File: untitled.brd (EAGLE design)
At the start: 54 x 54 mm, 26 parts, among them IC1 SN65220DBV, J3 CORTEX_DEBUG_PTH, J4 2X6 FEMALE, J6 USB-MICROB, U1 ATSAMD21G-M, U2 MIC5501-3.0YM5-TR, Y1 32.768kHz

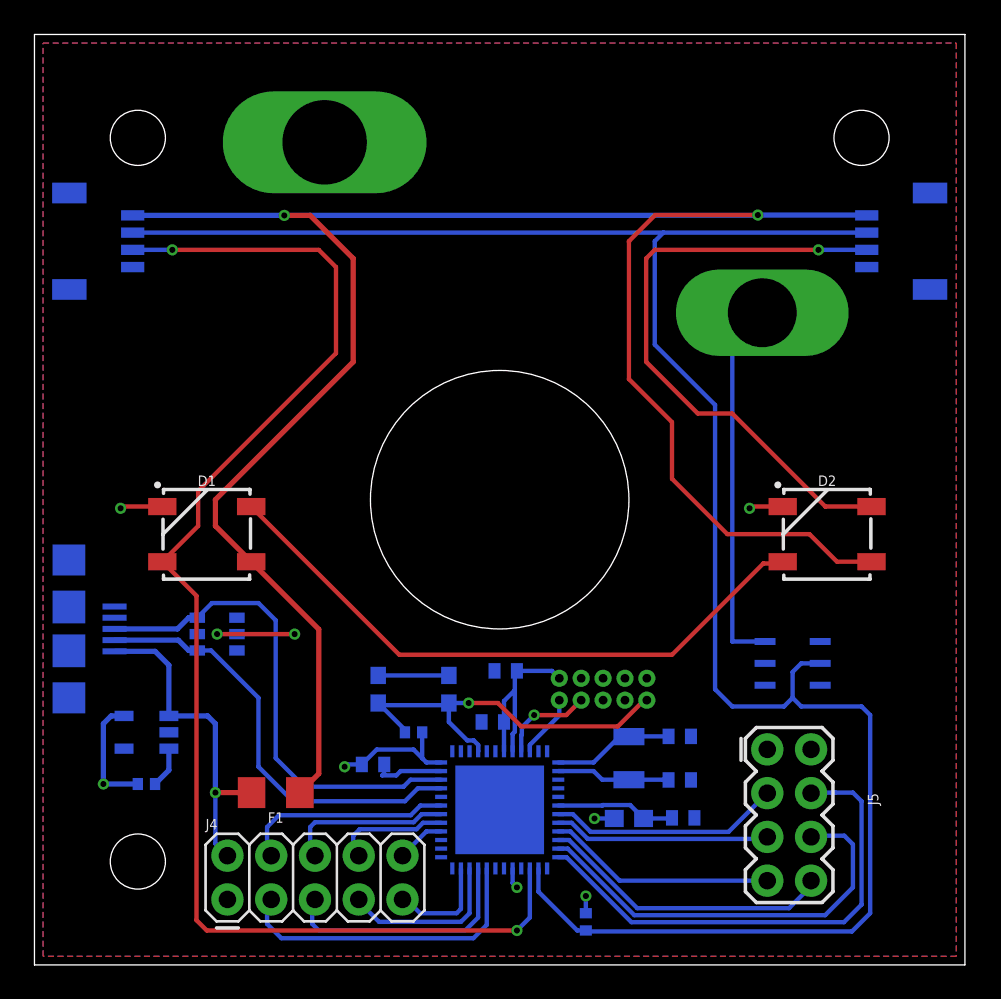
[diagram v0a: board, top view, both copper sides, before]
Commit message: corrected button orientation
placed novelkey on the correct side. reduced gpio by 2 pins to allow for tolerances. added mounting hole. updated routing.
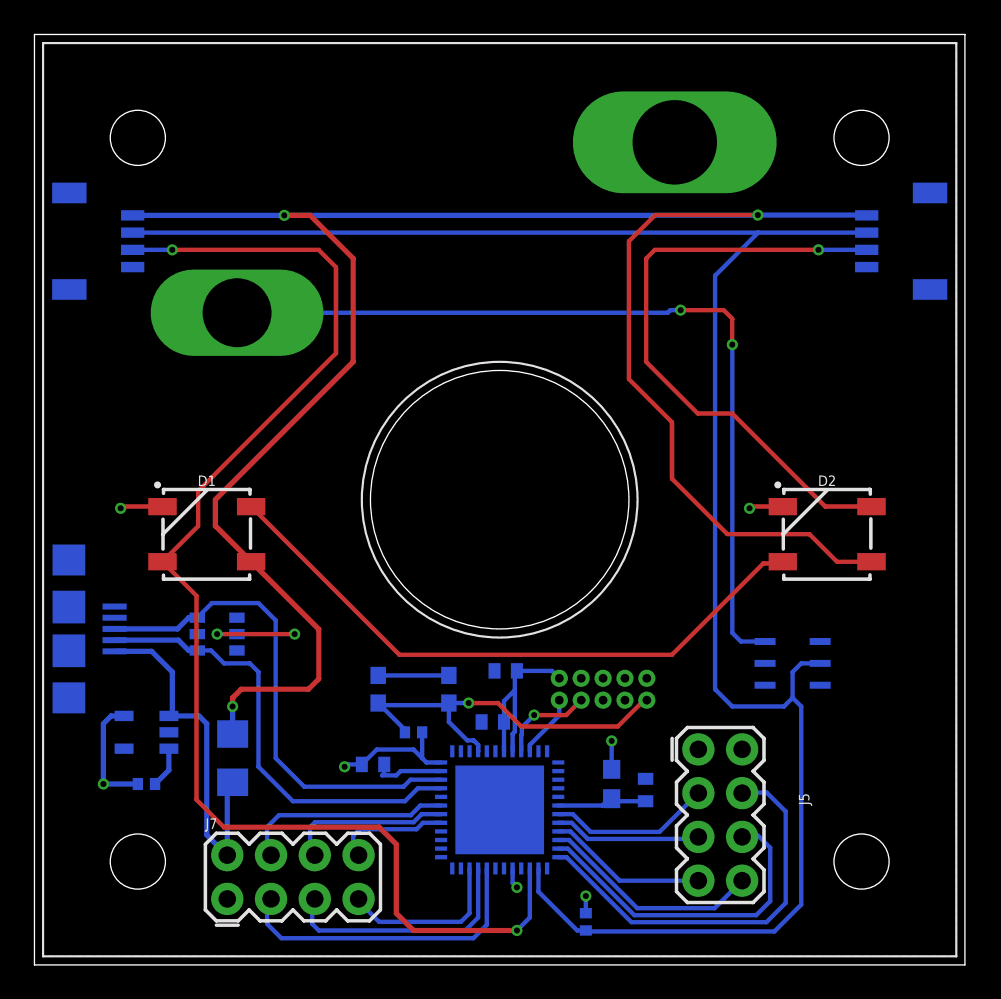
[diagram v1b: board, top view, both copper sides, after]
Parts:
- removed C4, C5: 12.5pf, resistor:C0402
- removed J4: 2X6 FEMALE, SparkFun-Connectors:2X5
- removed Y1: 32.768kHz, SparkFun-Clocks-custom:CRYSTAL-SMD-3.2X1.5MM
- added J7: (no value), SparkFun-Connectors:2X4
- moved J5 4.00 mm to (39.8, 8.70)
- moved F1 3.20 mm to (11.5, 12.0), flipped to the bottom, turned to 270 degrees
- moved C3 2.72 mm to (35.5, 10.2), turned to 90 degrees
- moved FB1 2.24 mm to (33.5, 10.5), turned to 270 degrees
- flipped U$1 to the top
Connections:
- removed net N$5: C4.1, U1.1, Y1.P$2
- removed net N$6: C5.1, U1.2, Y1.P$1
- removed net PA14: J4.9, U1.23
- removed net PA19: J4.10, U1.28
- net GND: now also J7.1; no longer C4.2, C5.2, J4.1
- net PA12: now also J7.5; no longer J4.5
- net PA13: now also J7.7; no longer J4.7
- net PA20: now also J7.8; no longer J4.8
- net PA21: now also J7.6; no longer J4.6
- net PA22: now also J7.4; no longer J4.4
- net PB11: now also J7.3; no longer J4.3
- net VBUS: now also J7.2; no longer J4.2
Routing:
- net N$10: track 21.7 -> 49.3 mm, vias 0 -> 2
- net 1W: track 117.6 -> 109.0 mm
- net N$5: track 7.03 -> 0.00 mm
- net N$6: track 6.61 -> 0.00 mm
- net PA14: track 6.17 -> 0.00 mm
- net PA06: track 24.5 -> 19.3 mm
- net PA07: track 28.7 -> 23.5 mm
- net PA05: track 17.2 -> 13.0 mm
- net PA09: track 12.6 -> 8.57 mm
- net PA08: track 13.5 -> 9.49 mm
- net PA04: track 13.3 -> 9.31 mm
- net PA19: track 2.84 -> 0.00 mm
- net VBUS: track 19.4 -> 21.8 mm, vias 1 -> 0
- net DIO: track 77.9 -> 76.1 mm
- net N$4: track 6.95 -> 5.57 mm
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
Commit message: updated silkscreen
updated silkscreen
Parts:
- R1: value (none) -> 10k
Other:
- board text added: "reset"
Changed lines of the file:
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@@
 <hole x="6" y="48" drill="3.2"/>
 <hole x="48" y="6" drill="3.2"/>
+<text x="24" y="18" size="1.27" layer="26" rot="MR0">reset</text>
+<text x="53" y="33.5" size="1.778" layer="26" rot="MR0">OUTPUT</text>
+<text x="1.2" y="33.8" size="1.778" layer="26" rot="MR180">INPUT</text>
+<text x="2.8" y="38.3" size="1.778" layer="25" rot="R90">INPUT</text>
+<text x="53" y="37" size="1.778" layer="25" rot="R90">OUTPUT</text>
 </plain>
 <attributes>
@@
 </element>
 <element name="U$2" library="1wire" package="TSOC6" value="DS2413P" x="44" y="17.5" smashed="yes" rot="MR270">
-<attribute name="NAME" x="41.46" y="20.04" size="1.27" layer="26" rot="MR270"/>
-<attribute name="VALUE" x="47.81" y="20.04" size="1.27" layer="28" rot="MR270"/>
+<attribute name="NAME" x="41.46" y="20.04" size="0.8128" layer="26" rot="MR270"/>
+<attribute name="VALUE" x="47.81" y="20.04" size="0.8128" layer="28" rot="MR270"/>
 </element>
 <element name="U1" library="SparkFun-IC-Microcontroller" library_urn="urn:adsk.eagle:library:525" package="QFN-48" package3d_urn="urn:adsk.eagle:package:38962/1" value="ATSAMD21G-M" x="27" y="9" smashed="yes" rot="MR0">
-<attribute name="NAME" x="27" y="13.445" size="0.6096" layer="26" font="vector" ratio="20" rot="MR0" align="bottom-center"/>
+<attribute name="NAME" x="24" y="12.945" size="0.6096" layer="26" font="vector" ratio="20" rot="MR0" align="bottom-center"/>
 <attribute name="PROD_ID" value="IC-13064" x="27" y="9" size="1.778" layer="28" rot="MR0" display="off"/>
 <attribute name="VALUE" x="32.08" y="9" size="0.6096" layer="28" font="vector" ratio="20" rot="MR270" align="bottom-center"/>
 </element>
-<element name="R1" library="rcl" library_urn="urn:adsk.eagle:library:334" package="R0402" package3d_urn="urn:adsk.eagle:package:23547/2" value="" x="22" y="13.5" smashed="yes" rot="MR180">
-<attribute name="NAME" x="21.365" y="12.865" size="1.27" layer="26" rot="MR180"/>
+<element name="R1" library="rcl" library_urn="urn:adsk.eagle:library:334" package="R0402" package3d_urn="urn:adsk.eagle:package:23547/2" value="10k" x="22" y="13.5" smashed="yes" rot="MR180">
+<attribute name="NAME" x="21.365" y="12.865" size="0.8128" layer="26" rot="MR180"/>
 <attribute name="SPICEPREFIX" value="R" x="22" y="13.5" size="1.778" layer="28" rot="MR180" display="off"/>
-<attribute name="VALUE" x="21.365" y="15.405" size="1.27" layer="28" rot="MR180"/>
+<attribute name="VALUE" x="18.865" y="13.405" size="0.8128" layer="28" rot="MR180"/>
 </element>
 <element name="C1" library="resistor" library_urn="urn:adsk.eagle:library:348" package="C0402" package3d_urn="urn:adsk.eagle:package:26136/1" value=".1f" x="26.6" y="14.1" smashed="yes" rot="MR0">
-<attribute name="NAME" x="27.489" y="14.862" size="1.27" layer="26" rot="MR0"/>
-<attribute name="VALUE" x="27.489" y="12.068" size="1.27" layer="28" rot="MR0"/>
+<attribute name="NAME" x="28.489" y="14.862" size="0.8128" layer="26" rot="MR0"/>
+<attribute name="VALUE" x="26.389" y="17.868" size="0.8128" layer="28" rot="MR0"/>
 </element>
 <element name="C2" library="resistor" library_urn="urn:adsk.eagle:library:348" package="C0402" package3d_urn="urn:adsk.eagle:package:26136/1" value=".1f" x="27.35" y="17.065" smashed="yes" rot="MR0">
-<attribute name="NAME" x="28.239" y="17.827" size="1.27" layer="26" rot="MR0"/>
-<attribute name="VALUE" x="28.239" y="15.033" size="1.27" layer="28" rot="MR0"/>
+<attribute name="NAME" x="28.239" y="17.827" size="0.8128" layer="26" rot="MR0"/>
+<attribute name="VALUE" x="27.039" y="14.833" size="0.8128" layer="28" rot="MR0"/>
 </element>
 <element name="C3" library="resistor" library_urn="urn:adsk.eagle:library:348" package="C0402" package3d_urn="urn:adsk.eagle:package:26136/1" value=".1f" x="35.465" y="10.15" smashed="yes" rot="MR90">
-<attribute name="NAME" x="34.727" y="6.261" size="1.27" layer="26" rot="MR90"/>
-<attribute name="VALUE" x="34.933" y="11.761" size="1.27" layer="28" rot="MR90"/>
+<attribute name="NAME" x="34.727" y="6.261" size="0.8128" layer="26" rot="MR90"/>
+<attribute name="VALUE" x="34.933" y="11.761" size="0.8128" layer="28" rot="MR90"/>
 </element>
 <element name="C6" library="resistor" library_urn="urn:adsk.eagle:library:348" package="C0402" package3d_urn="urn:adsk.eagle:package:26136/1" value=".1f" x="19.65" y="11.635" smashed="yes" rot="MR180">
-<attribute name="NAME" x="18.761" y="10.873" size="1.27" layer="26" rot="MR180"/>
-<attribute name="VALUE" x="18.761" y="13.667" size="1.27" layer="28" rot="MR180"/>
+<attribute name="NAME" x="20.261" y="10.873" size="0.8128" layer="26" rot="MR180"/>
+<attribute name="VALUE" x="18.661" y="10.867" size="0.8128" layer="28" rot="MR180"/>
 </element>
 <element name="FB1" library="SparkFun-Coils" library_urn="urn:adsk.eagle:library:512" package="0603" package3d_urn="urn:adsk.eagle:package:37574/1" value="30Ω/1.8A" x="33.5" y="10.5" smashed="yes" rot="MR270">
@@
 <attribute name="NAME" x="22" y="14.476" size="0.6096" layer="26" font="vector" ratio="20" rot="MR180" align="bottom-center"/>
 <attribute name="PROD_ID" value="SWCH-13065" x="22" y="16" size="1.778" layer="28" rot="MR180" display="off"/>
-<attribute name="VALUE" x="22" y="17.524" size="0.6096" layer="28" font="vector" ratio="20" rot="MR180" align="top-center"/>
 </element>
 <element name="R2" library="rcl" library_urn="urn:adsk.eagle:library:334" package="R0402" package3d_urn="urn:adsk.eagle:package:23547/2" value="4.7k" x="32" y="2.5" smashed="yes" rot="MR90">
-<attribute name="NAME" x="32.635" y="1.865" size="1.27" layer="26" rot="MR90"/>
+<attribute name="NAME" x="32.635" y="1.865" size="0.8128" layer="26" rot="MR90"/>
 <attribute name="SPICEPREFIX" value="R" x="32" y="2.5" size="1.778" layer="28" rot="MR90" display="off"/>
-<attribute name="VALUE" x="30.095" y="1.865" size="1.27" layer="28" rot="MR90"/>
+<attribute name="VALUE" x="30.595" y="1.865" size="0.8128" layer="28" rot="MR90"/>
 </element>
 <element name="IC1" library="sn65220_40" package="SOT23-6" value="SN65220DBV" x="10.6" y="19.2" smashed="yes" rot="MR270">
 <attribute name="NAME" x="8.898" y="20.597" size="1.016" layer="26" ratio="10" rot="MR270"/>
-<attribute name="VALUE" x="13.272" y="20.597" size="1.016" layer="28" ratio="10" rot="MR270"/>
+<attribute name="VALUE" x="7.772" y="17.597" size="0.8128" layer="28" ratio="10" rot="MR180"/>
 </element>
 <element name="F1" library="SparkFun-Fuses" library_urn="urn:adsk.eagle:library:517" package="1206" package3d_urn="urn:adsk.eagle:package:38575/1" value="6V/0.5A" x="11.5" y="12" smashed="yes" rot="MR270">
@@
 </element>
 <element name="R3" library="rcl" library_urn="urn:adsk.eagle:library:334" package="R0402" package3d_urn="urn:adsk.eagle:package:23547/2" value="10k" x="6.5" y="10.5" smashed="yes" rot="MR0">
-<attribute name="NAME" x="7.135" y="11.135" size="1.27" layer="26" rot="MR0"/>
+<attribute name="NAME" x="8.135" y="8.635" size="0.8128" layer="26" rot="MR0"/>
 <attribute name="SPICEPREFIX" value="R" x="6.5" y="10.5" size="1.778" layer="28" rot="MR0" display="off"/>
-<attribute name="VALUE" x="7.135" y="8.595" size="1.27" layer="28" rot="MR0"/>
+<attribute name="VALUE" x="6.135" y="8.595" size="0.8128" layer="28" rot="MR0"/>
 </element>
 <element name="J5" library="SparkFun-Connectors" library_urn="urn:adsk.eagle:library:513" package="2X4" package3d_urn="urn:adsk.eagle:package:38103/1" value="" x="39.8" y="8.7" smashed="yes" rot="R270">

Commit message: added esp version and removed led
added an esp8266 version of the board. Removed an LED from the samd21g version to move the LED to the empty space on the bottom of the novelkey.
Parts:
- removed D1: WS2812B, SparkFun-LED:WS2812B
- moved D2 24.8 mm to (27.0, 9.00)
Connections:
- removed net N$11: D1.2, D2.4
- net 5V: no longer D1.1
- net DIO: now also D2.4; no longer D1.4
- net GND: no longer D1.3
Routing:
- net N$11: track 36.6 -> 0.00 mm
- net DO: track 35.6 -> 50.0 mm
- net GND: track 16.7 -> 29.2 mm, vias 4 -> 2
- net DIO: track 76.1 -> 69.1 mm

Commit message: added vias below usb
added gnd vias below the USB connector to improve mechanical stability.
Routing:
- net GND: track 29.2 -> 40.6 mm, vias 2 -> 12
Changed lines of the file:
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@@
 <setting verticaltext="up"/>
 </settings>
-<grid distance="0.5" unitdist="mm" unit="mm" style="lines" multiple="1" display="no" altdistance="0.1" altunitdist="mm" altunit="mm"/>
+<grid distance="0.5" unitdist="mm" unit="mm" style="lines" multiple="1" display="no" altdistance="0.05" altunitdist="mm" altunit="mm"/>
 <layers>
 <layer number="1" name="Top" color="4" fill="1" visible="yes" active="yes"/>
@@
 <wire x1="16.9" y1="10.6" x2="15.1" y2="12.4" width="0.254" layer="1"/>
 <wire x1="15.1" y1="12.4" x2="15.1" y2="19.2" width="0.254" layer="1"/>
+<via x="2" y="18.2" extent="1-16" drill="0.35"/>
+<via x="2.6" y="18.8" extent="1-16" drill="0.35"/>
+<via x="1.4" y="17.65" extent="1-16" drill="0.35"/>
+<via x="2.6" y="17.65" extent="1-16" drill="0.35"/>
+<via x="2.6" y="20.2" extent="1-16" drill="0.35"/>
+<via x="1.4" y="20.2" extent="1-16" drill="0.35"/>
+<via x="2" y="20.75" extent="1-16" drill="0.35"/>
+<via x="1.4" y="21.35" extent="1-16" drill="0.35"/>
+<via x="2.6" y="21.35" extent="1-16" drill="0.35"/>
+<wire x1="2.6" y1="17.65" x2="2.05" y2="18.2" width="0.254" layer="1"/>
+<wire x1="2.05" y1="18.2" x2="2" y2="18.2" width="0.254" layer="1"/>
+<wire x1="2" y1="18.2" x2="2.6" y2="18.8" width="0.254" layer="1"/>
+<wire x1="2.6" y1="18.8" x2="2.6" y2="20.2" width="0.254" layer="1"/>
+<wire x1="2.6" y1="20.2" x2="2.05" y2="20.75" width="0.254" layer="1"/>
+<wire x1="2.05" y1="20.75" x2="2" y2="20.75" width="0.254" layer="1"/>
+<wire x1="2" y1="20.75" x2="1.4" y2="21.35" width="0.254" layer="1"/>
+<wire x1="2.6" y1="21.35" x2="2.05" y2="20.8" width="0.254" layer="1"/>
+<wire x1="2.05" y1="20.8" x2="2.05" y2="20.75" width="0.254" layer="1"/>
+<via x="1.4" y="18.8" extent="1-16" drill="0.35"/>
+<wire x1="1.4" y1="20.2" x2="1.4" y2="18.8" width="0.254" layer="1"/>
+<wire x1="1.4" y1="20.2" x2="1.95" y2="20.75" width="0.254" layer="1"/>
+<wire x1="1.95" y1="20.75" x2="2" y2="20.75" width="0.254" layer="1"/>
+<wire x1="2" y1="18.2" x2="1.45" y2="17.65" width="0.254" layer="1"/>
+<wire x1="1.45" y1="17.65" x2="1.4" y2="17.65" width="0.254" layer="1"/>
+<wire x1="2" y1="18.2" x2="1.4" y2="18.8" width="0.254" layer="1"/>
+<wire x1="2.6" y1="21.35" x2="2.75" y2="21.5" width="0.254" layer="16"/>
+<wire x1="2.75" y1="21.5" x2="4.5" y2="21.5" width="0.254" layer="16"/>
 </signal>
 <signal name="1W">
